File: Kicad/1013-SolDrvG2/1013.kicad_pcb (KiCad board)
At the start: 2 copper layers, 44.5 x 20.3 mm, 16 parts, among them P1 TST, P10 SPADE_187, P2 CONN_4, P3 CONN_4, P4 CONN2X3MOLEX, P5 CONN_4, P6 CONN_8, Q1 MOSFET_N, Q2 MOSFET_N, Q3 MOSFET_N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

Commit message: Updates to silkscreen and created mashup.  These Gerbers sent to PCB house.
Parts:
- R1, R5: value 100K -> 0
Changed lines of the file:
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@@
     (links 34)
     (no_connects 0)
-    (area 222.2754 188.0235 270.3322 211.9122)
+    (area 223.444999 189.956396 268.325601 211.421133)
     (thickness 1.6)
     (drawings 8)
@@
   )
   (setup
-    (last_trace_width 1.27)
+    (last_trace_width 0.254)
     (user_trace_width 0.635)
     (user_trace_width 0.889)
@@
       (effects (font (size 0.762 0.762) (thickness 0.1524)))
     )
-    (fp_text value 100K (at -1.143 2.54) (layer F.SilkS) hide
+    (fp_text value 0 (at 0 0) (layer F.SilkS) hide
       (effects (font (size 1.397 1.27) (thickness 0.2032)))
     )
@@
       (effects (font (size 0.762 0.762) (thickness 0.1524)))
     )
-    (fp_text value 100K (at -1.143 2.54 180) (layer F.SilkS) hide
-      (effects (font (size 1.397 1.27) (thickness 0.2032)))
-    )
+    (fp_text value 0 (at -1.143 2.54 180) (layer F.SilkS) hide
+      (effects (font (size 1.397 1.27) (thickness 0.2032)))
+    )

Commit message: Added OPP logo to all boards.  Better late than never.
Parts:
- added VAL: REF, opp_logo_backsilk, F.Cu at (261.0, 208.3)

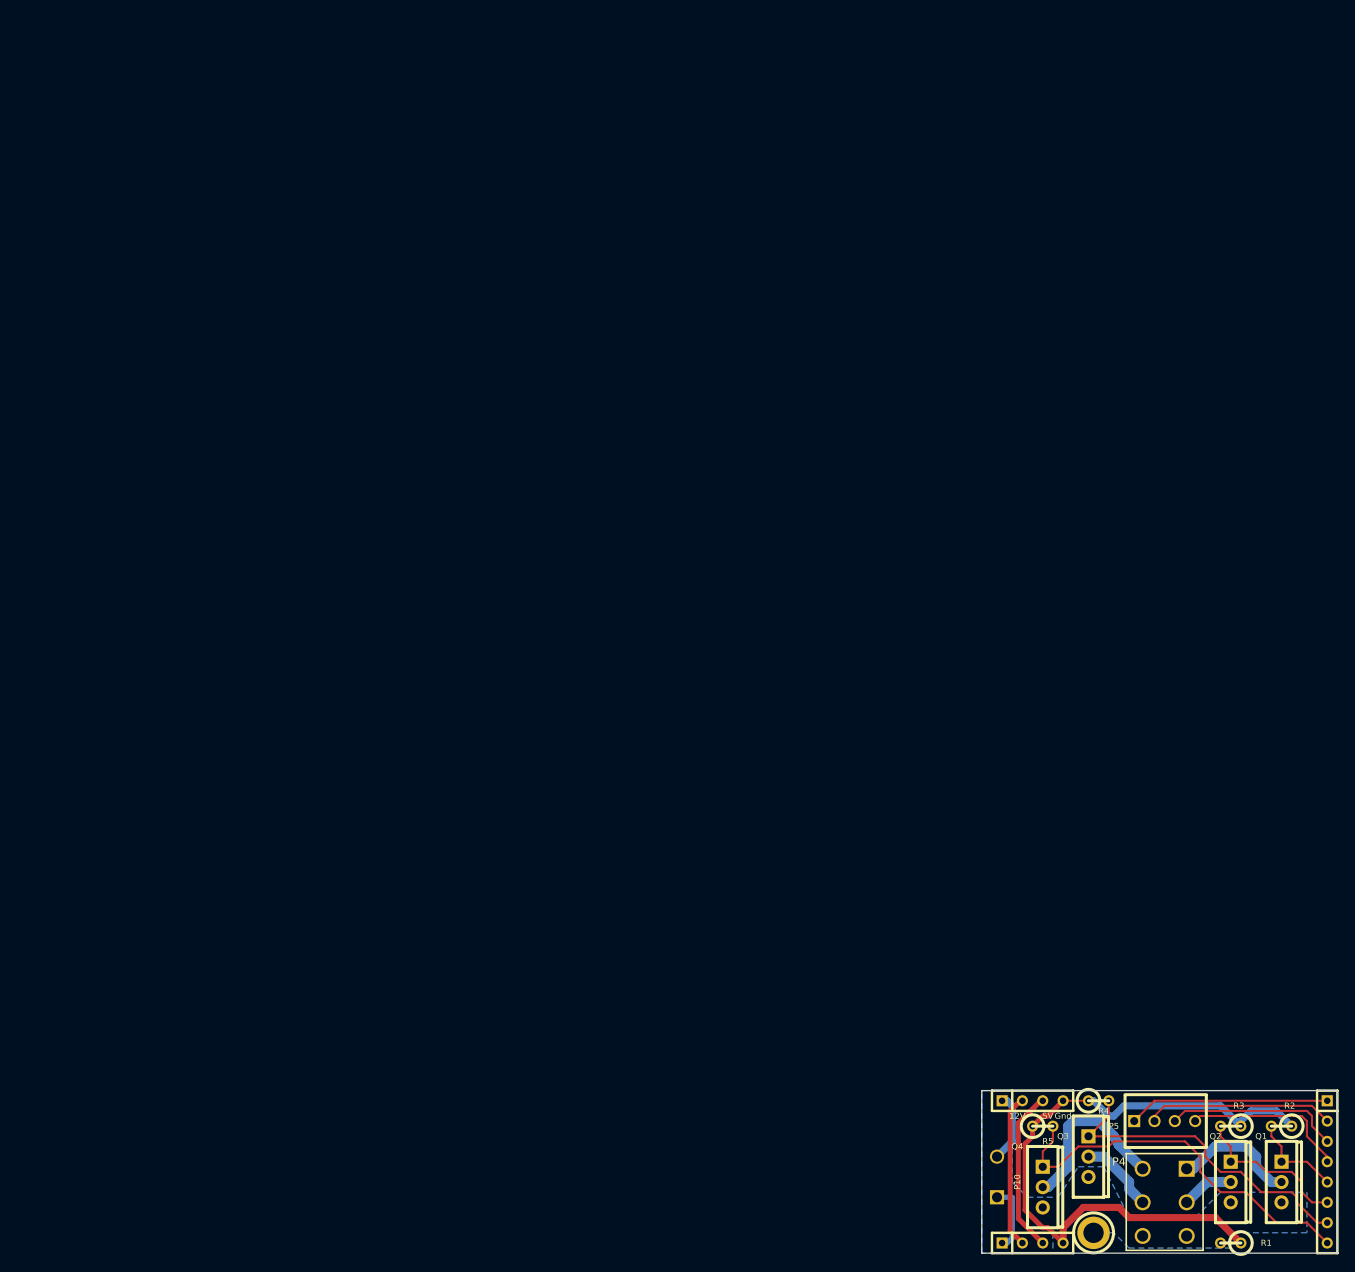
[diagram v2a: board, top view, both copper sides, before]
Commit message: Changed size of PCB sheets to 8.5" x 11".  Added name/rev/board name to PCB sheets.
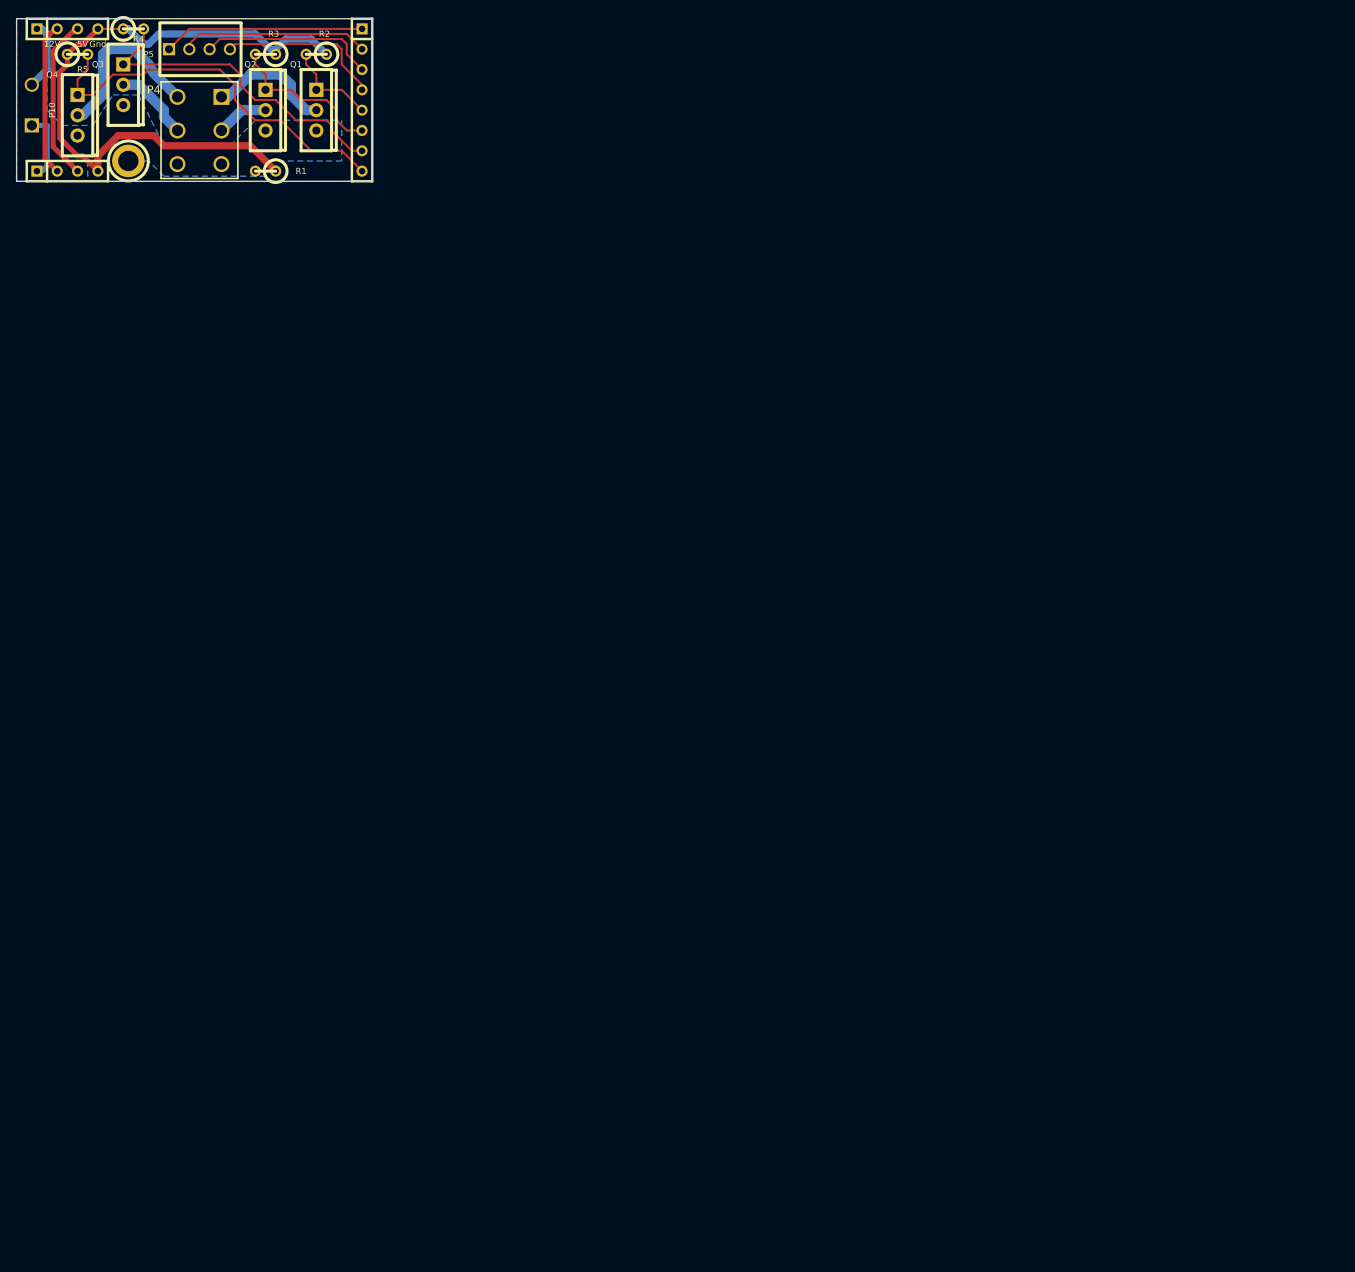
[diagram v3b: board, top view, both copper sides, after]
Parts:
- moved P1 180.3 mm to (116.8, 74.3)
- moved P10 180.3 mm to (104.8, 67.3)
- moved P2 180.3 mm to (109.2, 57.8)
- moved P3 180.3 mm to (109.2, 75.6)
- moved P4 180.3 mm to (125.7, 70.5)
- moved P5 180.3 mm to (125.7, 60.3)
- moved P6 180.3 mm to (146.1, 66.7)
- moved Q1 180.3 mm to (140.3, 67.9)
- moved Q2 180.3 mm to (134.0, 67.9)
- moved Q3 180.3 mm to (116.2, 64.8)
- moved Q4 180.3 mm to (110.5, 68.6)
- moved R1 180.3 mm to (134.0, 75.6)
- moved R2 180.3 mm to (140.3, 61.0)
- moved R4 180.3 mm to (117.5, 57.8)
- moved R5 180.3 mm to (110.5, 61.0)
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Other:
- board size 44.5 x 20.3 mm -> 44.4 x 20.3 mm

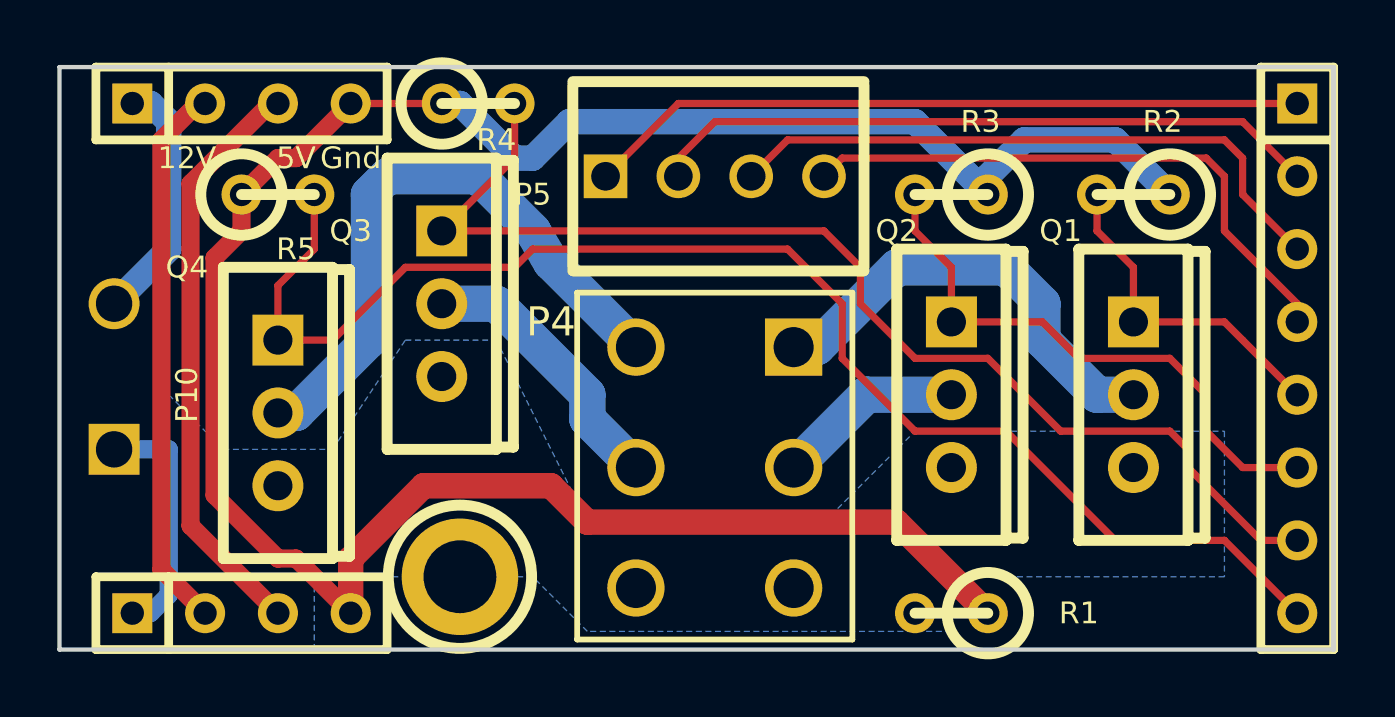
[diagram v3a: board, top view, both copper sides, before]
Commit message: Gen2 embedded code: Remove debug code that always overwrites NV configuration.  Added Gen2.rev0.1.1.0.cyacd for downloading to boards.
PopulateBrd document:
Correct solenoid pinout picture.

SolDrvG2 board:
Move location of 4 pin switch input header to reduce interference with interface board.  Update to use cheaper 6 pin Molex header.  Add rev to copper layer.

IntfBrdG2 board:
Change future pin on ribbon cable connector to carry 12V.  Make board slightly larger so it can be panellized by IteadStudio.  Add better grounding.  Move ribbon cable connectors so less interference with solenoid board input header.  Add 3 pin header to make communicating with first board in chain easier (switch comms between 4 pin header and ribbon cable).  Add rev to copper layer.

IncandSMG2 board:
Update to use cheaper 2 pin Molex header.  Add rev to copper layer.

Panellize Gerbers:
Add panellized boards for SolDrvG2, IntfBrdG2, and IncandSMG2.

MPF/SS3:
Small updates to add skillshot.
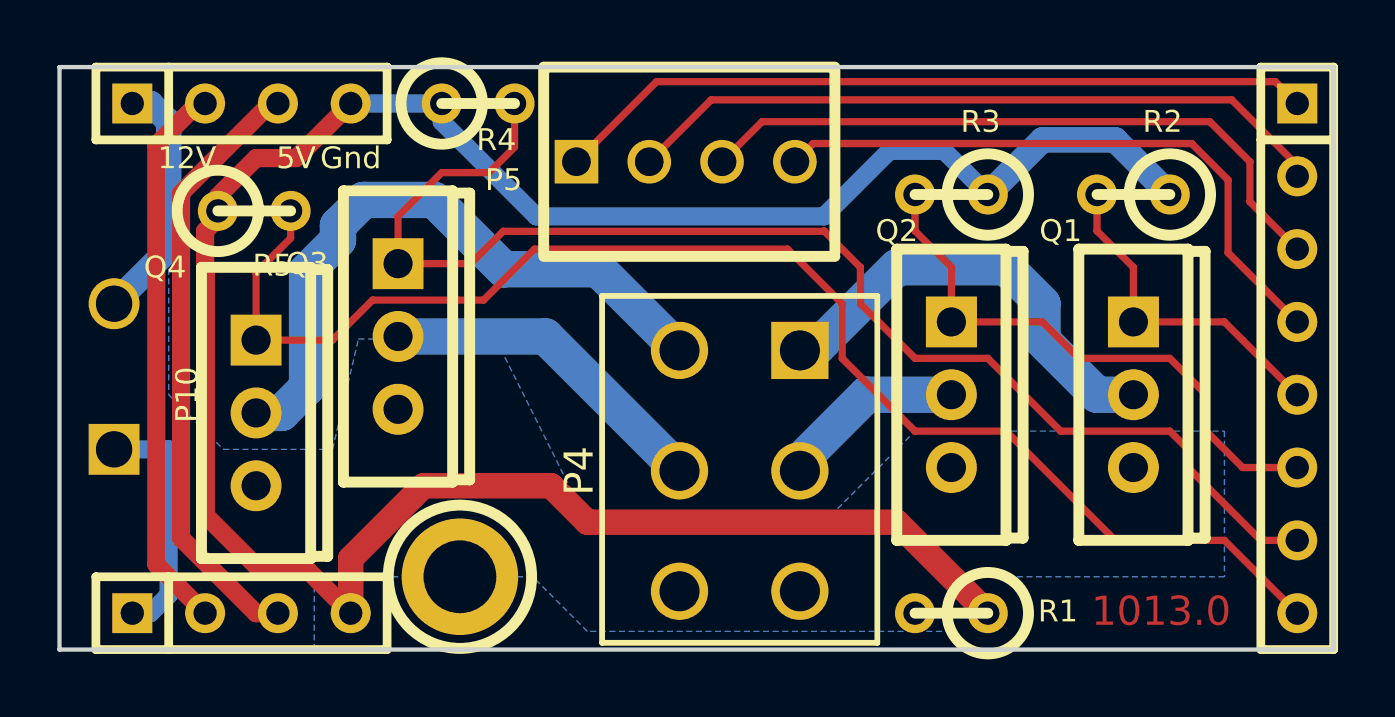
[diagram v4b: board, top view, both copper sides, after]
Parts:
- P4: footprint 00_th2x3x4.2mm_nopeg -> 00_th2x3x4.2mm_cheap
- R5: value 0 -> 100K
- moved Q3 1.91 mm to (114.7, 65.9)
- moved P5 1.14 mm to (124.7, 59.8)
- moved R5 1.00 mm to (109.7, 61.5)
- moved P4 0.88 mm to (126.6, 70.6)
- moved Q4 0.76 mm to (109.7, 68.6)
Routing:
- net /P6: track 40.9 -> 45.7 mm
- net GND: track 82.4 -> 84.5 mm
- net N-0000012: track 9.64 -> 11.8 mm
- net /P0: track 25.2 -> 26.6 mm
- net /P2: track 21.9 -> 23.3 mm
- net /P1: track 23.5 -> 24.8 mm
- net /P3: track 20.6 -> 21.9 mm
- net N-000008: track 21.5 -> 22.7 mm
- net +5V: track 20.5 -> 21.2 mm
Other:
- rule trace_min: 0.254 -> 0.2032
- rule via_min_drill: 0.508 -> 0.3048
- rule via_min_size: 0.889 -> 0.635
- board text added: "1013.0"
